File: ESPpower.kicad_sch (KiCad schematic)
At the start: 58 parts, among them CON1 +7 TO +20VDC, J1 RJ12, J2 Display, J3 Conn_01x02_Male, J4 Conn_01x02_Male, M1 ESP-12, P1 Program, Q1 AO3400, SW1 Reset, SW2 Program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

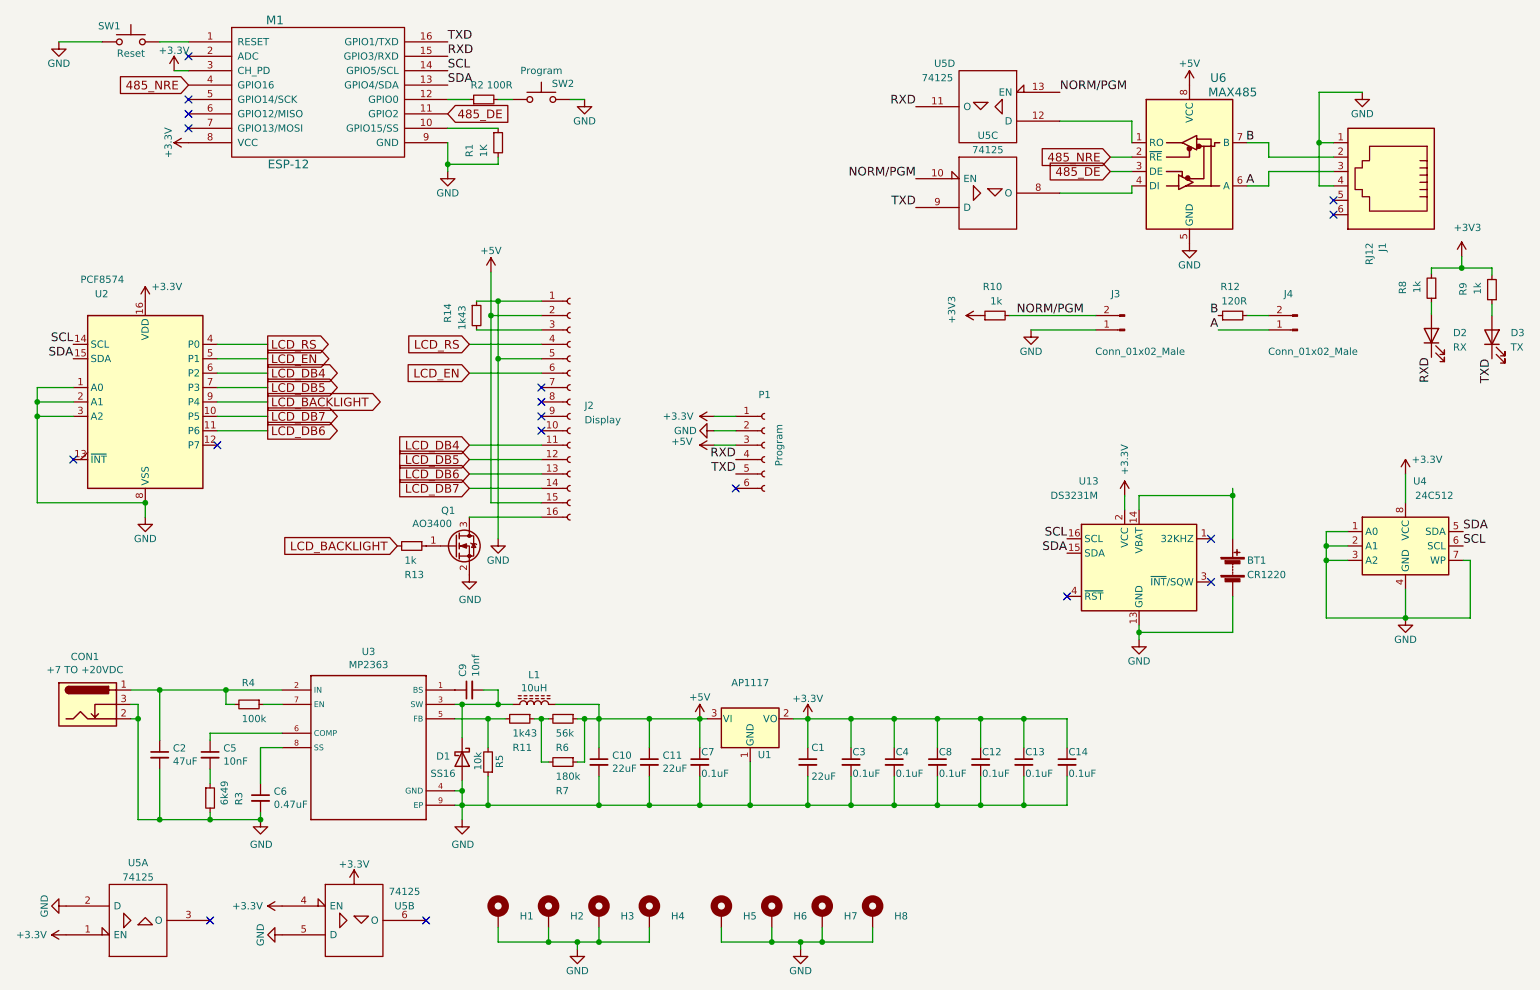
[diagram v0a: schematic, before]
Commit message: Fix U4 part number to FM24C256 Fix U1 part to AP1117-3.3
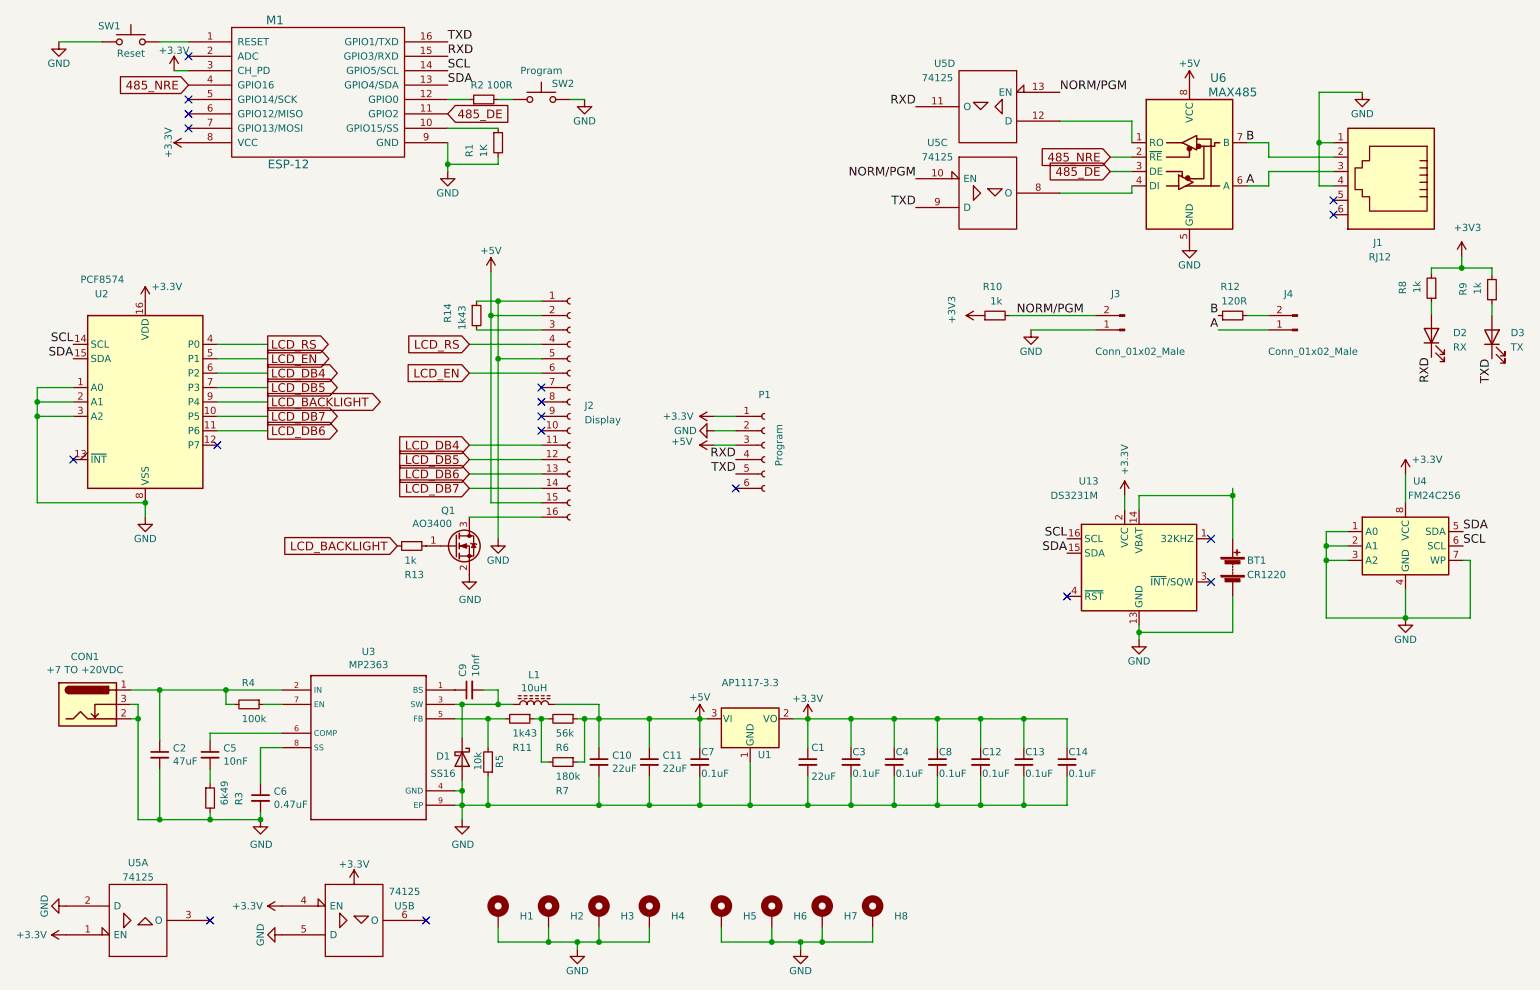
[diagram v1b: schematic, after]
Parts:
- U1: value AP1117 -> AP1117-3.3
- U4: value 24C512 -> FM24C256
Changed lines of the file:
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@@
     (in_bom yes) (on_board yes)
     (property "Reference" "U1" (id 0) (at 146.05 151.13 0))
-    (property "Value" "AP1117" (id 1) (at 143.51 138.43 0))
+    (property "Value" "AP1117-3.3" (id 1) (at 143.51 138.43 0))
     (property "Footprint" "Package_TO_SOT_SMD:SOT-223-3_TabPin2" (id 2) (at 143.51 139.7 0)
       (effects (font (size 1.27 1.27)) hide)
@@
   (symbol (lib_id "Connector:6P6C") (at 256.54 48.26 180) (unit 1)
     (in_bom yes) (on_board yes)
-    (property "Reference" "J1" (id 0) (at 255.016 60.8076 90)
+    (property "Reference" "J1" (id 0) (at 255.016 60.8076 0)
       (effects (font (size 1.27 1.27)) (justify left))
     )
-    (property "Value" "RJ12" (id 1) (at 252.7046 60.8076 90)
+    (property "Value" "RJ12" (id 1) (at 256.5146 63.3476 0)
       (effects (font (size 1.27 1.27)) (justify left))
     )
@@
     (in_bom yes) (on_board yes)
     (property "Reference" "U4" (id 0) (at 261.62 102.87 0))
-    (property "Value" "24C512" (id 1) (at 264.16 105.41 0))
+    (property "Value" "FM24C256" (id 1) (at 264.16 105.41 0))
     (property "Footprint" "Package_SO:SOIC-8_5.23x5.23mm_P1.27mm" (id 2) (at 259.08 114.3 0)
       (effects (font (size 1.27 1.27)) hide)
@@
   )
   (symbol (lib_id "74xx_IEEE:74125") (at 185.42 52.07 0) (unit 3)
-    (in_bom yes) (on_board yes) (fields_autoplaced)
-    (property "Reference" "U5" (id 0) (at 185.42 41.91 0))
-    (property "Value" "74125" (id 1) (at 185.42 44.45 0))
+    (in_bom yes) (on_board yes)
+    (property "Reference" "U5" (id 0) (at 176.53 43.18 0))
+    (property "Value" "74125" (id 1) (at 176.53 45.72 0))
     (property "Footprint" "Package_SO:SOIC-14_3.9x8.7mm_P1.27mm" (id 2) (at 185.42 52.07 0)
       (effects (font (size 1.27 1.27)) hide)
@@
     )
     (path "/00000000-0000-0000-0000-0000562afafe"
-      (reference "U1") (unit 1) (value "AP1117") (footprint "Package_TO_SOT_SMD:SOT-223-3_TabPin2")
+      (reference "U1") (unit 1) (value "AP1117-3.3") (footprint "Package_TO_SOT_SMD:SOT-223-3_TabPin2")
     )
     (path "/00000000-0000-0000-0000-0000562e1ac8"
@@
     )
     (path "/00000000-0000-0000-0000-00005743ac5e"
-      (reference "U4") (unit 1) (value "24C512") (footprint "Package_SO:SOIC-8_5.23x5.23mm_P1.27mm")
+      (reference "U4") (unit 1) (value "FM24C256") (footprint "Package_SO:SOIC-8_5.23x5.23mm_P1.27mm")
     )
     (path "/79c358be-0155-40d3-b1fd-0ca5d5e8b16d"
